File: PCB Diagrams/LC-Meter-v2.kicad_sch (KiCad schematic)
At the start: 32 parts, among them J1 Power, J2 External, J3 Cx/Lx, J4 GND, J5 Display I2C, J6 Base 01, J7 Top 01, J8 Base 02, J9 Top 02, SW1 Select, SW2 High, SW3 Med, SW4 Low, U1 LM358

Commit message: first commit
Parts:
- added J10: Ext/A, Connector_PinHeader_2.54mm:PinHeader_1x01_P2.54mm_Horizontal, symbol Connector:Conn_01x01_Pin
- added J11: Ext/B, Connector_PinHeader_2.54mm:PinHeader_1x01_P2.54mm_Horizontal, symbol Connector:Conn_01x01_Pin
- J6: value Base 01 -> CxMode/A
- J7: value Top 01 -> CxMode/B
- J8: value Base 02 -> Select/A
- J9: value Top 02 -> Select/B
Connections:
- net GND: now also J2.2 (Pin_2)
- net at J5.2 (Pin_2): now also A1.23 (A4); no longer A1.25 (A6)
- net at J5.3 (Pin_3): now also A1.24 (A5); no longer A1.26 (A7)
- net at C1.1, J8.1 (Pin_1), R5.1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: no longer J2.2 (Pin_2)
- net at J3.1 (Pin_1), J3.2 (Pin_2), J3.3 (Pin_3)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: now also J10.1 (Pin_1)
- net at A1.19 (A0), J8.2 (Pin_2), R1.1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: no longer J2.1 (Pin_1)
- new net: J11.1 (Pin_1), J2.1 (Pin_1)
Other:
- moved on the sheet: A1, C1, H1, H2, H3, H4, H5, H6, H7, H8, H9, J1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

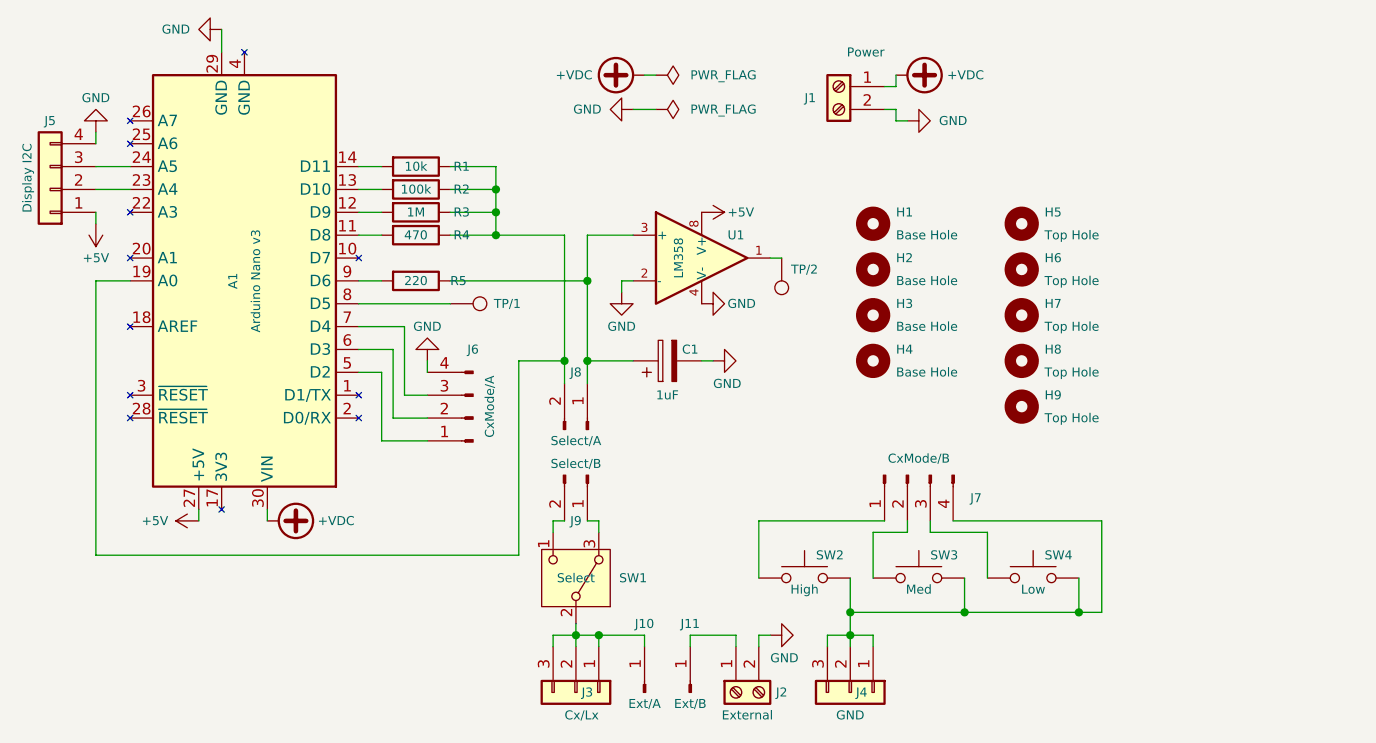
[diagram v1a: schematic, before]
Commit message: pin position & component annotations improvements
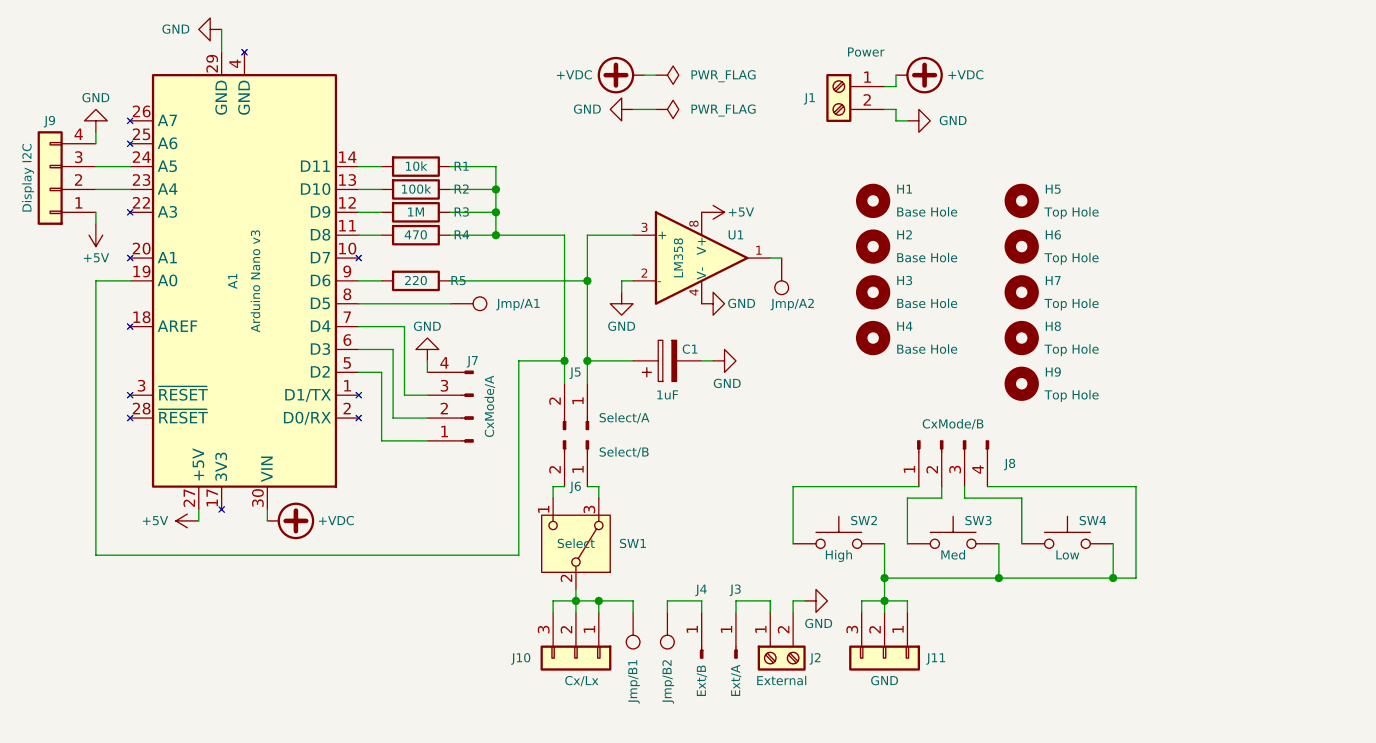
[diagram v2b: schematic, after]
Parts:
- added Jmp/B1, Jmp/B2: Bridge, TestPoint:TestPoint_THTPad_D2.0mm_Drill1.0mm, symbol Connector:TestPoint
- J3: renamed from J11; value Ext/B -> Ext/A
- J4: renamed from J10; value Ext/A -> Ext/B
- renumbered J3 to J10, J4 to J11, J8 to J5, J9 to J6, J6 to J7, J7 to J8, J5 to J9, TP/1 to Jmp/A1, TP/2 to Jmp/A2
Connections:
- net at J10.1 (Pin_1), J10.2 (Pin_2), J10.3 (Pin_3)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: now also Jmp/B1.1; no longer J4.1 (Pin_1)
- new net: J4.1 (Pin_1), Jmp/B2.1
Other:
- moved on the sheet: H1, H2, H3, H4, H5, H6, H7, H8, H9, J10, J11, J2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
